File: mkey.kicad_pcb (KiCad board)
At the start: 2 copper layers, 346.1 x 94.5 mm, 161 parts, among them J1 USB_C_REP_2.0, U1 ESP32-S3-WROOM-1, U2 SY8088

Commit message: initial schematic updates for routing matrix
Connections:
- U1 pad 15: unconnected-(U1-GPIO3/TOUCH3/ADC1_CH2-Pad15) -> ROW3
- U1 pad 16: unconnected-(U1-GPIO46-Pad16) -> ROW4
- U1 pad 18: unconnected-(U1-GPIO10/TOUCH10/ADC1_CH9/FSPICS0/FSPIIO4/SUBSPICS0-Pad18) -> COL13
- U1 pad 19: unconnected-(U1-GPIO11/TOUCH11/ADC2_CH0/FSPID/FSPIIO5/SUBSPID-Pad19) -> COL12
- U1 pad 20: unconnected-(U1-GPIO12/TOUCH12/ADC2_CH1/FSPICLK/FSPIIO6/SUBSPICLK-Pad20) -> COL11
- U1 pad 21: unconnected-(U1-GPIO13/TOUCH13/ADC2_CH2/FSPIQ/FSPIIO7/SUBSPIQ-Pad21) -> COL10
- U1 pad 22: unconnected-(U1-GPIO14/TOUCH14/ADC2_CH3/FSPIWP/FSPIDQS/SUBSPIWP-Pad22) -> COL9
- U1 pad 23: unconnected-(U1-GPIO21-Pad23) -> COL8
- U1 pad 24: unconnected-(U1-GPIO47/SPICLK_P/SUBSPICLK_P_DIFF-Pad24) -> COL7
- U1 pad 25: unconnected-(U1-GPIO48/SPICLK_N/SUBSPICLK_N_DIFF-Pad25) -> COL6
- U1 pad 26: unconnected-(U1-GPIO45-Pad26) -> ROW2
- U1 pad 28: unconnected-(U1-SPIIO6/GPIO35/FSPID/SUBSPID-Pad28) -> ROW1
- U1 pad 29: unconnected-(U1-SPIIO7/GPIO36/FSPICLK/SUBSPICLK-Pad29) -> COL5
- U1 pad 30: unconnected-(U1-SPIDQS/GPIO37/FSPIQ/SUBSPIQ-Pad30) -> COL4
- U1 pad 31: unconnected-(U1-GPIO38/FSPIWP/SUBSPIWP-Pad31) -> COL3
- U1 pad 36: unconnected-(U1-U0RXD/GPIO44/CLK_OUT2-Pad36) -> COL2
- U1 pad 37: unconnected-(U1-U0TXD/GPIO43/CLK_OUT1-Pad37) -> COL1
- U1 pad 38: unconnected-(U1-GPIO2/TOUCH2/ADC1_CH1-Pad38) -> COL0
- U1 pad 39: unconnected-(U1-GPIO1/TOUCH1/ADC1_CH0-Pad39) -> ROW0

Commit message: routed entire keyboard matrix
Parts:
- D69: moved to B.Cu
- turned D69 to 180 degrees
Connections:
- U1 pad 15: ROW3 -> unconnected-(U1-GPIO3/TOUCH3/ADC1_CH2-Pad15)
- U1 pad 17: unconnected-(U1-GPIO9/TOUCH9/ADC1_CH8/FSPIHD/SUBSPIHD-Pad17) -> ROW3
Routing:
- net COL0: track 82.4 -> 363.4 mm, vias 0 -> 1
- net COL1: track 87.7 -> 349.4 mm, vias 0 -> 1
- net COL2: track 89.7 -> 332.1 mm, vias 0 -> 1
- net COL3: track 67.7 -> 290.4 mm, vias 0 -> 1
- net COL4: track 67.7 -> 270.3 mm, vias 0 -> 1
- net COL5: track 101.8 -> 284.3 mm, vias 0 -> 1
- net COL6: track 67.7 -> 238.9 mm, vias 0 -> 1
- net COL7: track 137.0 -> 291.0 mm, vias 0 -> 1
- net COL8: track 134.8 -> 275.6 mm, vias 0 -> 1
- net COL9: track 141.4 -> 264.6 mm, vias 0 -> 1
- net COL10: track 145.7 -> 251.6 mm, vias 0 -> 1
- net COL11: track 152.4 -> 241.0 mm, vias 0 -> 1
- net ROW4: track 326.2 -> 396.3 mm, vias 0 -> 2
- net ROW3: track 307.2 -> 363.3 mm
- net COL12: track 133.8 -> 184.1 mm, vias 0 -> 1
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
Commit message: Add mounting holes, route usb
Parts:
- added ?: , , F.Cu at (272.3, 108.7)
- added ?: , , F.Cu at (57.1, 122.2)
- added ?: , , F.Cu at (158.8, 100.8)
- added ?: , , F.Cu at (60.3, 70.6)
- added REF**: MountingHole_3.2mm_M3_DIN965_Pad, MountingHole:MountingHole_3.2mm_M3_DIN965_Pad, F.Cu at (377.0, 49.2)
- moved D69 8.56 mm to (362.4, 56.4), turned to 0 degrees
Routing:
- net USB_D-: track 0.00 -> 39.8 mm, vias 0 -> 1
- net USB_D+: track 0.00 -> 39.4 mm, vias 0 -> 1
- added copper zone on F.Cu, net GND

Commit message: place and route buttons
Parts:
- BOOT_SW1, C2, C8, R7, RESET_SW1: moved to B.Cu
- moved BOOT_SW1 68.5 mm to (306.4, 72.2), turned to 90 degrees
- moved C8 59.5 mm to (309.2, 70.9)
- moved R7 57.4 mm to (311.2, 69.3)
- moved RESET_SW1 28.0 mm to (350.0, 57.3), turned to 180 degrees
- moved C2 26.1 mm to (355.4, 48.9), turned to 180 degrees
- moved R2 5.25 mm to (355.8, 54.5)
- moved D69 1.12 mm to (363.5, 56.4)
- moved C3 0.36 mm to (346.7, 53.4)
- moved C7 0.36 mm to (343.8, 49.6)
- moved D67 0.36 mm to (355.5, 46.5)
- moved R1 0.36 mm to (340.6, 53.4)
- moved R3 0.36 mm to (348.6, 53.5)
- moved R4 0.36 mm to (352.5, 53.5)
- moved U2 0.36 mm to (355.8, 51.8)
- moved D68 0.36 mm to (345.9, 49.5)
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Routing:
- net CHIP_POWER: track 17.9 -> 53.9 mm, vias 0 -> 2
- net USB_D-: track 39.8 -> 6.53 mm
- net USB_D+: track 39.4 -> 6.81 mm
- net BOOT: track 0.00 -> 18.5 mm, vias 0 -> 2
- net CHIP_PU: track 5.25 -> 16.6 mm
- net VBUS: track 6.09 -> 10.9 mm
- net Net-(U2-FB): track 9.17 -> 12.9 mm
- net Net-(U2-EN): track 5.13 -> 1.84 mm
- removed copper zone on F.Cu, net GND

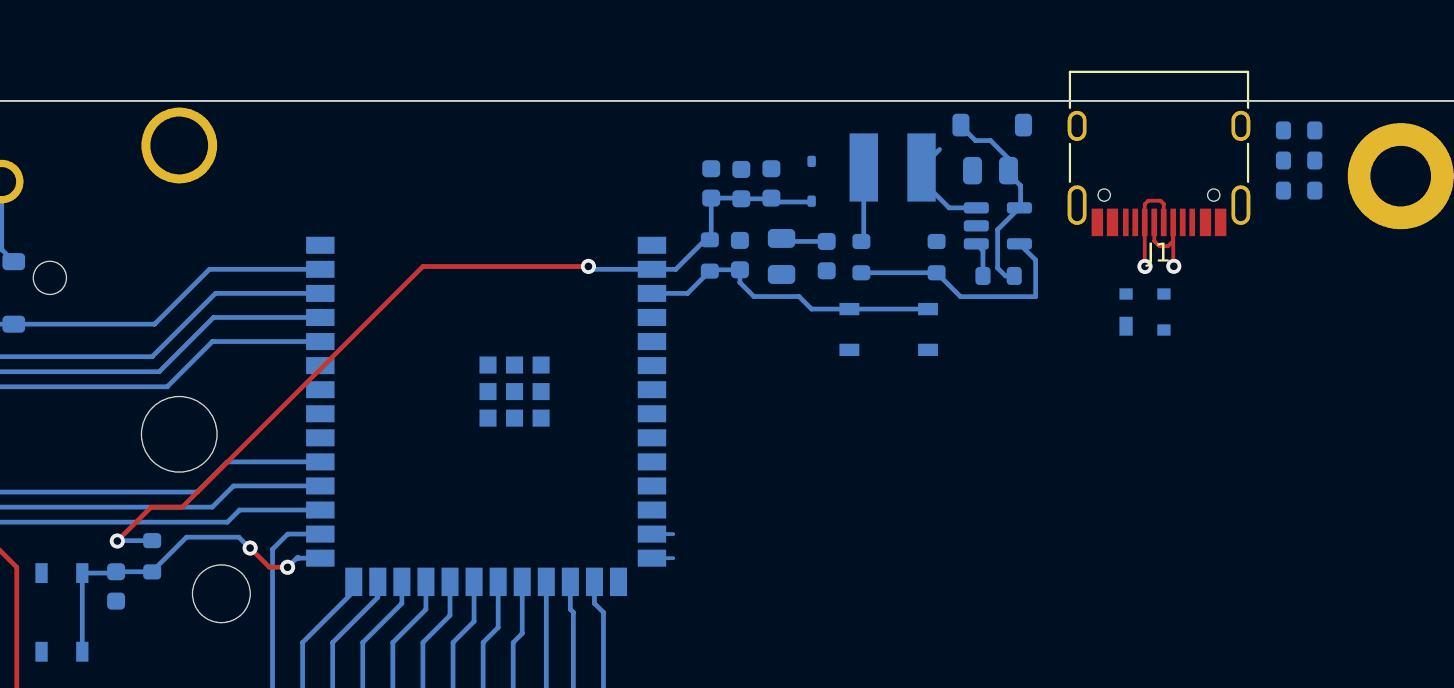
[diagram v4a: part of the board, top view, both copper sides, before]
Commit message: all nets connected, basic drc passing, now just edge violations
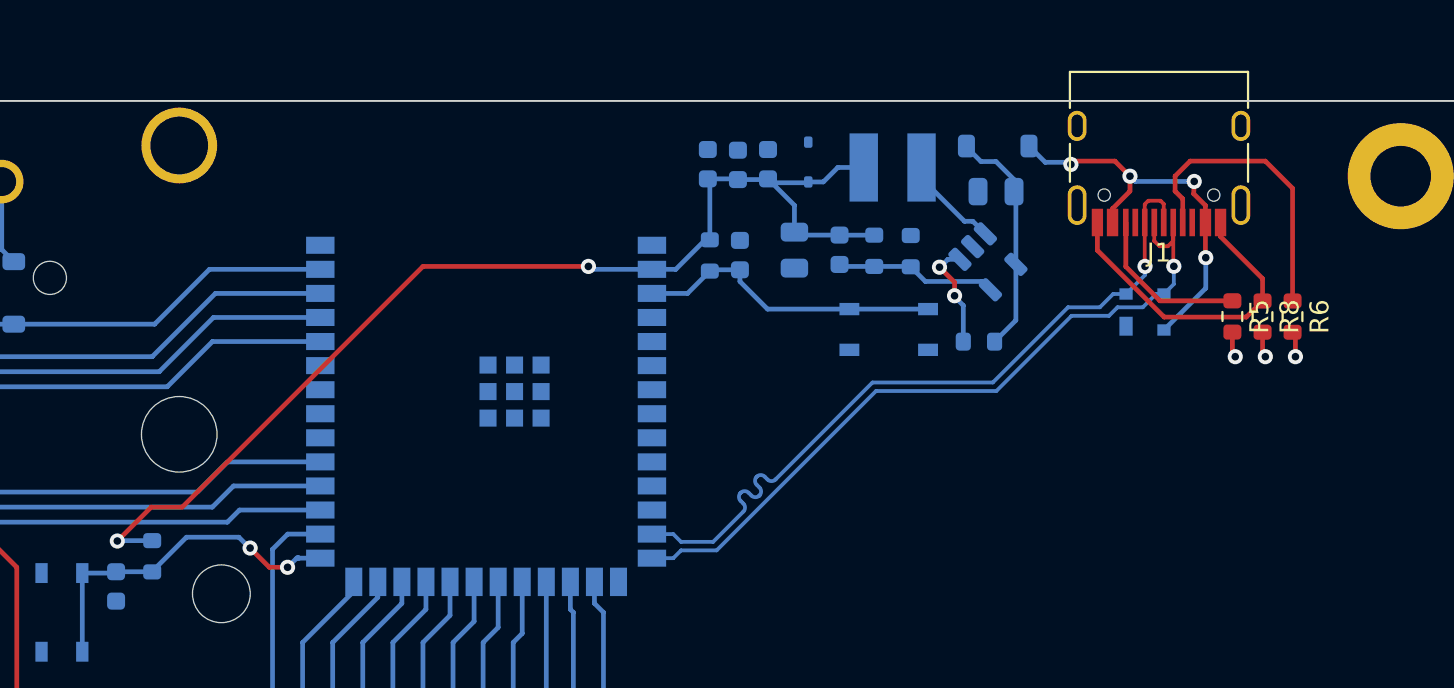
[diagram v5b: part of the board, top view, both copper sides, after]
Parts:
- R5, R6, R8: moved to F.Cu
- moved R6 9.83 mm to (371.3, 56.6), turned to -90 degrees
- moved R8 8.46 mm to (369.7, 56.6), turned to -90 degrees
- moved R5 7.52 mm to (368.1, 56.6), turned to -90 degrees
- moved R2 3.62 mm to (354.8, 57.9)
- moved U2 1.97 mm to (355.2, 53.7), turned to -45 degrees
- moved R4 1.40 mm to (351.2, 53.2)
- moved D67 1.14 mm to (355.8, 47.6)
- moved C2 1.14 mm to (355.7, 50.0)
- moved D68 1.03 mm to (345.8, 48.5)
- moved C5 1.03 mm to (340.5, 48.6)
- moved C6 1.03 mm to (342.1, 48.6)
- moved C7 1.03 mm to (343.6, 48.6)
- moved C3 0.76 mm to (347.4, 53.1)
- moved R3 0.76 mm to (349.2, 53.1)
- moved C4 0.76 mm to (345.0, 53.1)
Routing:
- net USB_D-: track 6.53 -> 40.0 mm
- net USB_D+: track 6.81 -> 40.2 mm
- net Net-(D67-A): track 0.00 -> 21.6 mm, vias 0 -> 4
- net Net-(J1-GND-PadA1): track 0.00 -> 17.1 mm
- net Net-(J1-CC1): track 0.00 -> 15.7 mm
- net Net-(J1-CC2): track 0.00 -> 8.70 mm
- net CHIP_POWER: track 53.9 -> 59.7 mm
- net Net-(U2-FB): track 12.9 -> 8.57 mm
- net GND: track 0.15 -> 4.21 mm, vias 0 -> 3
- net Net-(U2-EN): track 1.84 -> 5.88 mm, vias 0 -> 2
- net VBUS: track 10.9 -> 12.5 mm
- net /Buck_Coil: track 5.51 -> 6.52 mm

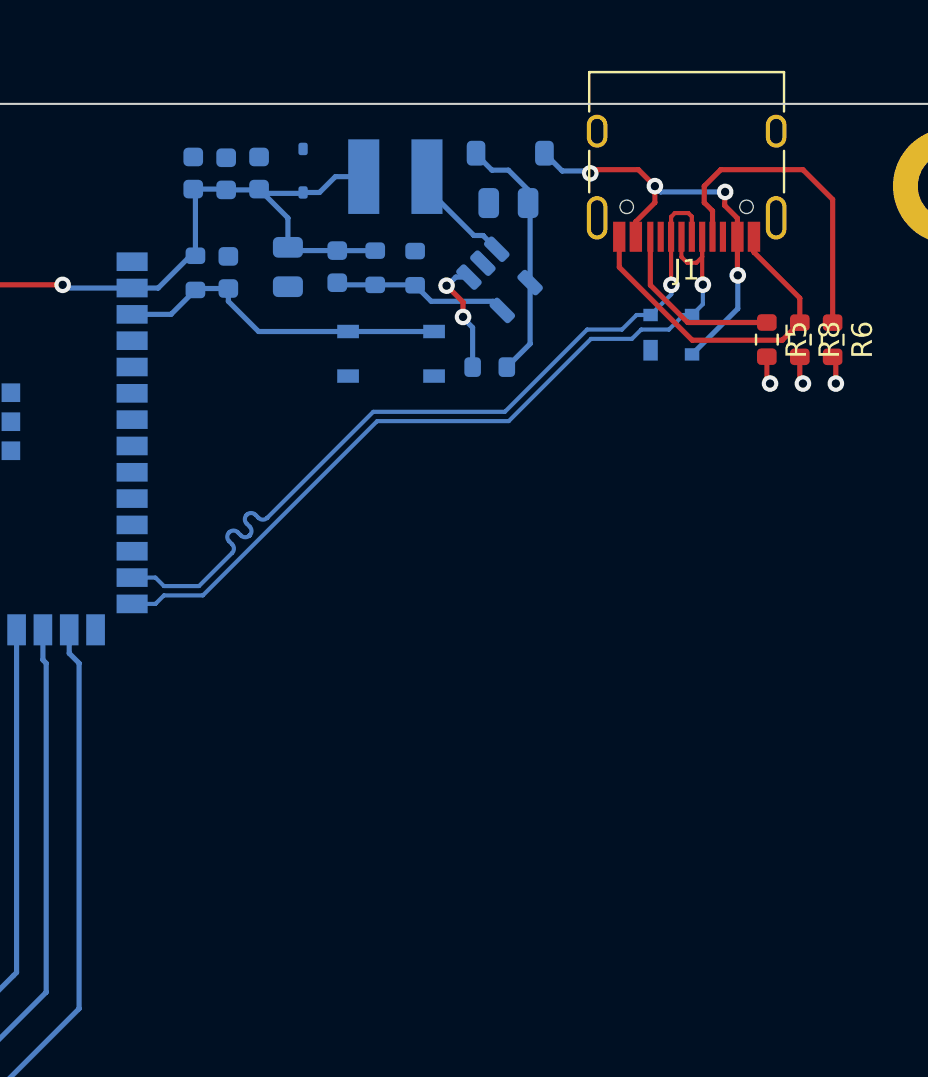
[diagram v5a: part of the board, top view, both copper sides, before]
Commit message: Add display connector to schematic, thicken power traces
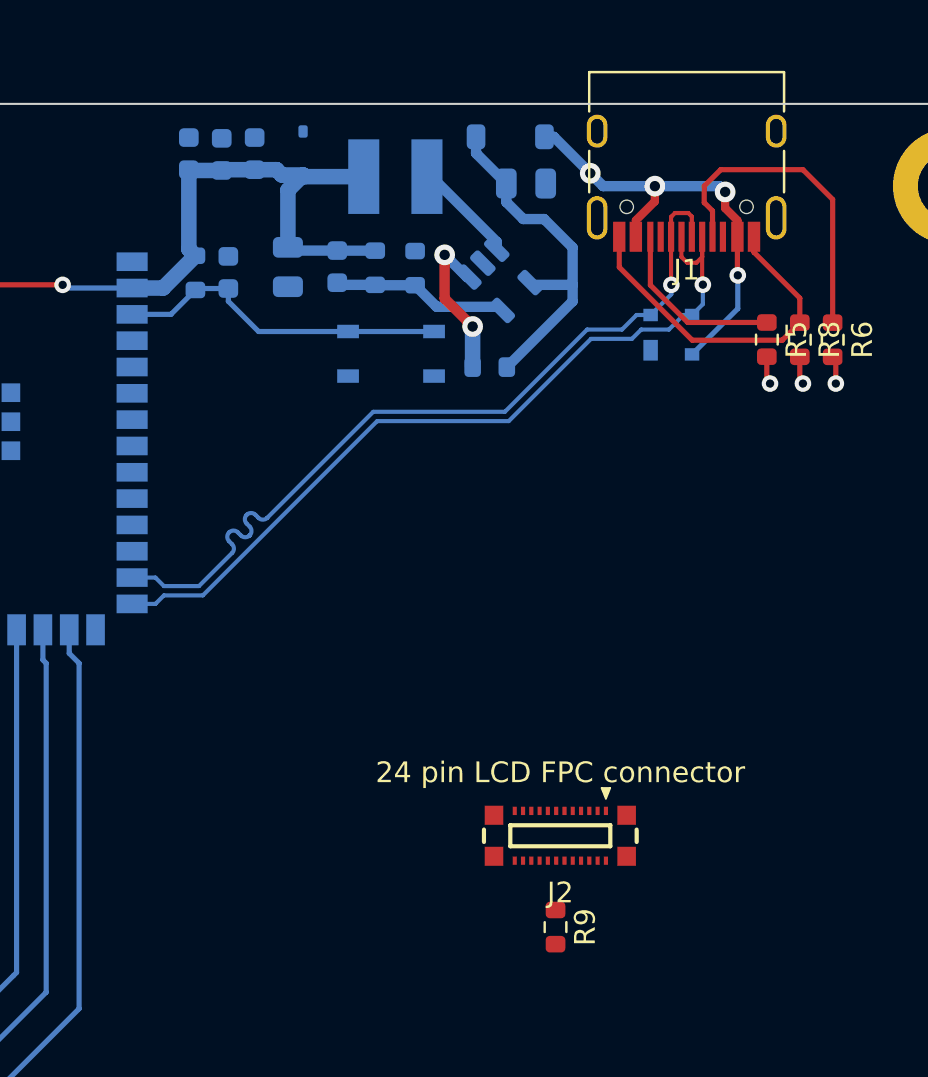
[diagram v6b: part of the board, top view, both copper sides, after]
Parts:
- added J2: 24 pin LCD FPC connector, CONN-SMD_24P-P0.40__X0400FVS-24-LPSN:CONN-SMD_24P-P0.40_X0400FVS-24-LPSN, F.Cu at (358.2, 80.6)
- added R9: 51.1R 1%, Resistor_SMD:R_0603_1608Metric, F.Cu at (357.9, 85.0)
- moved C2 1.27 mm to (356.5, 49.1), turned to 0 degrees
- moved C5 0.96 mm to (340.3, 47.6)
- moved C6 0.96 mm to (341.8, 47.7)
- moved C7 0.96 mm to (343.4, 47.6)
- moved D68 0.84 mm to (345.8, 47.6)
- moved D67 0.79 mm to (355.8, 46.8)
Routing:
- net VBUS: track 12.5 -> 17.2 mm
- net CHIP_POWER: track 59.7 -> 62.2 mm
- net Net-(U2-EN): track 5.88 -> 7.64 mm
- net Net-(D67-A): track 21.6 -> 22.2 mm
